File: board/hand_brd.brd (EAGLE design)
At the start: 61.9 x 76.2 mm, 131 parts, among them IC1 FT230XS, Q1 BC847ALT1SMD, Q2 16MHz, Q3 16MHz, U2 ATXMEGA128D4-AU

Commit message: Add missing diode
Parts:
- added U$26: PMEG2010ET, pol:SOT23
- moved R20 2.62 mm to (61.0, 24.1)
- moved R19 1.27 mm to (57.8, 21.6)
- moved Q2 1.27 mm to (54.0, 26.0)
- moved R17 0.90 mm to (60.3, 19.7), turned to 225 degrees
- moved R18 0.63 mm to (55.9, 21.6)
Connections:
- new net N$11: R20.2, U$26.3
- net N$14: now also U$26.1; no longer R20.2
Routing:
- net PDI_CK: track 32.3 -> 29.5 mm
- net N$11: track 0.00 -> 2.23 mm
- net P_XTAL1: track 6.74 -> 8.01 mm
- net P_3V3: track 28.0 -> 26.8 mm
- net N$14: track 13.4 -> 12.6 mm
- net PDI_DATA: track 28.9 -> 28.1 mm
- net N$13: track 10.0 -> 10.6 mm
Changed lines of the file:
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@@
 <element name="C12" library="rcl" package="C0805K" value="10u" x="57.785" y="6.985" smashed="yes" rot="MR180"/>
 <element name="R14" library="rcl" package="M0805" value="10k" x="46.355" y="17.78" smashed="yes" rot="R90"/>
-<element name="Q2" library="special" package="QS" value="16MHz" x="55.245" y="26.035" smashed="yes" rot="R180"/>
+<element name="Q2" library="special" package="QS" value="16MHz" x="53.975" y="26.035" smashed="yes" rot="R180"/>
 <element name="C14" library="rcl" package="C0805K" value="27p" x="52.705003125" y="23.495" smashed="yes" rot="MR180"/>
 <element name="C15" library="rcl" package="C0805K" value="27p" x="57.785003125" y="23.494996875" smashed="yes" rot="MR0"/>
@@
 <attribute name="VALUE" x="40.259" y="26.67" size="1.27" layer="27" ratio="10" rot="R270"/>
 </element>
-<element name="R17" library="rcl" package="M0805" value="10k" x="60.96" y="19.05" smashed="yes" rot="MR270"/>
-<element name="R18" library="rcl" package="M0805" value="100" x="56.515" y="21.59" smashed="yes" rot="R270"/>
-<element name="R19" library="rcl" package="M0805" value="100" x="59.055" y="21.59" smashed="yes" rot="R270"/>
-<element name="R20" library="rcl" package="M0805" value="100" x="61.595" y="21.59" smashed="yes" rot="R270"/>
+<element name="R17" library="rcl" package="M0805" value="10k" x="60.325" y="19.685" smashed="yes" rot="MR225"/>
+<element name="R18" library="rcl" package="M0805" value="100" x="55.88" y="21.59" smashed="yes" rot="R270"/>
+<element name="R19" library="rcl" package="M0805" value="100" x="57.785" y="21.59" smashed="yes" rot="R270"/>
+<element name="R20" library="rcl" package="M0805" value="100" x="60.96" y="24.13" smashed="yes" rot="R270"/>
 <element name="R21" library="rcl" package="M0805" value="10k" x="46.355" y="22.225" smashed="yes" rot="R270"/>
 <element name="R13" library="rcl" package="M0805" value="100" x="45.72" y="12.7" smashed="yes" rot="R90"/>
@@
 <element name="U1" library="MicroUSB" package="USB-MICRO-SMD" value="" x="52.07" y="73.025" rot="MR270"/>
 <element name="U3" library="MicroUSB" package="USB-MICRO-SMD" value="" x="53.975" y="1.905" rot="MR90"/>
+<element name="U$26" library="pol" package="SOT23" value="PMEG2010ET" x="60.96" y="20.32"/>
 </elements>
 <signals>
@@
 <via x="57.785" y="52.705" extent="1-16" drill="0.6"/>
 <via x="43.815" y="36.83" extent="1-16" drill="0.6"/>
-<via x="56.515" y="27.94" extent="1-16" drill="0.6"/>
+<via x="58.42" y="26.035" extent="1-16" drill="0.6"/>
 <contactref element="U1" pad="GND1"/>
 <wire x1="53.37" y1="70.325" x2="53.37" y2="69.82" width="0.4064" layer="16"/>
@@
 <contactref element="Q2" pad="1"/>
 <contactref element="U$13" pad="2"/>
-<wire x1="57.785" y1="26.035" x2="56.78500625" y2="25.035" width="0.4064" layer="16"/>
+<wire x1="56.515" y1="26.035" x2="56.78500625" y2="25.035" width="0.4064" layer="16"/>
 <wire x1="56.78500625" y1="25.035" x2="56.785003125" y2="23.494996875" width="0.4064" layer="16"/>
 <wire x1="55.596115625" y1="19.6895375" x2="56.785003125" y2="20.878428125" width="0.4064" layer="16"/>
@@
 <contactref element="Q2" pad="2"/>
 <contactref element="U$13" pad="1"/>
-<wire x1="52.705" y1="26.035" x2="53.705003125" y2="25.035" width="0.4064" layer="16"/>
-<wire x1="53.705003125" y1="25.035" x2="53.705003125" y2="23.495" width="0.4064" layer="16"/>
 <wire x1="55.030428125" y1="20.255225" x2="53.705003125" y2="21.580653125" width="0.4064" layer="16"/>
 <wire x1="53.705003125" y1="21.580653125" x2="53.705003125" y2="23.495" width="0.4064" layer="16"/>
+<wire x1="53.705003125" y1="23.495" x2="53.705003125" y2="25.034996875" width="0.4064" layer="16"/>
+<wire x1="53.705003125" y1="25.034996875" x2="52.705" y2="26.035" width="0.4064" layer="16"/>
+<wire x1="52.705" y1="26.035" x2="51.435" y2="26.035" width="0.4064" layer="16"/>
 </signal>
 <signal name="N$10">
@@
 <wire x1="46.675" y1="18.415" x2="48.26" y2="18.415" width="0.4064" layer="1"/>
 <wire x1="46.355" y1="21.275" x2="46.355" y2="18.73" width="0.4064" layer="1"/>
-<wire x1="56.727484375" y1="18.55816875" x2="58.169315625" y2="20" width="0.4064" layer="16"/>
-<wire x1="58.169315625" y1="20" x2="60.96" y2="20" width="0.4064" layer="16"/>
+<wire x1="56.727484375" y1="18.55816875" x2="58.526065625" y2="20.35675" width="0.4064" layer="16"/>
+<wire x1="58.526065625" y1="20.35675" x2="59.65325" y2="20.35675" width="0.4064" layer="16"/>
 </signal>
 <signal name="HWB">
@@
 <wire x1="59.410653125" y1="15.875" x2="59.69" y2="15.24" width="0.4064" layer="16"/>
 <via x="59.69" y="15.24" extent="1-16" drill="0.6"/>
-<wire x1="56.515" y1="20.64" x2="56.515" y2="19.05" width="0.4064" layer="1"/>
-<wire x1="56.515" y1="19.05" x2="59.69" y2="15.875" width="0.4064" layer="1"/>
 <wire x1="59.69" y1="15.875" x2="59.69" y2="15.24" width="0.4064" layer="1"/>
+<wire x1="55.88" y1="20.64" x2="55.88" y2="19.685" width="0.4064" layer="1"/>
+<wire x1="55.88" y1="19.685" x2="59.69" y2="15.875" width="0.4064" layer="1"/>
 </signal>
 <signal name="N$13">
@@
 <wire x1="59.8398" y1="13.335" x2="60.325" y2="13.335" width="0.4064" layer="16"/>
 <via x="60.325" y="13.335" extent="1-16" drill="0.6"/>
-<wire x1="59.055" y1="20.64" x2="59.055" y2="18.415" width="0.4064" layer="1"/>
-<wire x1="59.055" y1="18.415" x2="60.96" y2="16.51" width="0.4064" layer="1"/>
-<wire x1="60.96" y1="16.51" x2="60.96" y2="13.97" width="0.4064" layer="1"/>
+<wire x1="60.96" y1="15.875" x2="60.96" y2="13.97" width="0.4064" layer="1"/>
 <wire x1="60.96" y1="13.97" x2="60.325" y2="13.335" width="0.4064" layer="1"/>
+<wire x1="57.785" y1="20.64" x2="57.785" y2="19.05" width="0.4064" layer="1"/>
+<wire x1="57.785" y1="19.05" x2="60.96" y2="15.875" width="0.4064" layer="1"/>
 </signal>
 <signal name="PDI_DATA">
@@
 <contactref element="R19" pad="1"/>
 <contactref element="U2" pad="34"/>
-<wire x1="56.515" y1="22.54" x2="59.055" y2="22.54" width="0.4064" layer="1"/>
+<wire x1="55.88" y1="22.54" x2="57.785" y2="22.54" width="0.4064" layer="1"/>
 <wire x1="47.680353125" y1="41.90720625" x2="47.680353125" y2="42.489646875" width="0.4064" layer="1"/>
 <wire x1="47.680353125" y1="42.489646875" x2="46.99" y2="43.18" width="0.4064" layer="1"/>
@@
 <wire x1="46.99" y1="43.18" x2="46.99" y2="40.64" width="0.4064" layer="16"/>
 <via x="53.975" y="29.21" extent="1-16" drill="0.6"/>
-<wire x1="56.515" y1="22.54" x2="56.2" y2="22.54" width="0.4064" layer="1"/>
+<wire x1="55.88" y1="22.54" x2="56.2" y2="22.54" width="0.4064" layer="1"/>
 <wire x1="46.99" y1="40.64" x2="52.705" y2="34.925" width="0.4064" layer="16"/>
 <wire x1="52.705" y1="34.925" x2="52.705" y2="34.29" width="0.4064" layer="16"/>
 <wire x1="52.705" y1="34.29" x2="53.975" y2="33.02" width="0.4064" layer="16"/>
 <wire x1="53.975" y1="33.02" x2="53.975" y2="29.21" width="0.4064" layer="16"/>
-<wire x1="56.2" y1="22.54" x2="55.245" y2="23.495" width="0.4064" layer="1"/>
-<wire x1="55.245" y1="23.495" x2="55.245" y2="27.94" width="0.4064" layer="1"/>
+<wire x1="55.245" y1="23.175" x2="55.245" y2="27.94" width="0.4064" layer="1"/>
 <wire x1="55.245" y1="27.94" x2="53.975" y2="29.21" width="0.4064" layer="1"/>
+<wire x1="55.245" y1="23.175" x2="55.88" y2="22.54" width="0.4064" layer="1"/>
 </signal>
 <signal name="N$14">
 <contactref element="U$13" pad="11"/>
-<contactref element="R20" pad="2"/>
 <wire x1="57.85885625" y1="13.0532" x2="59.48205625" y2="11.43" width="0.4064" layer="16"/>
 <wire x1="59.48205625" y1="11.43" x2="59.69" y2="11.43" width="0.4064" layer="16"/>
 <via x="59.69" y="11.43" extent="1-16" drill="0.6"/>
-<wire x1="61.595" y1="20.64" x2="62.23" y2="20.005" width="0.4064" layer="1"/>
-<wire x1="62.23" y1="20.005" x2="62.23" y2="13.335" width="0.4064" layer="1"/>
+<wire x1="60.325" y1="11.43" x2="59.69" y2="11.43" width="0.4064" layer="1"/>
+<contactref element="U$26" pad="1"/>
+<wire x1="60.01" y1="19.22" x2="60.01" y2="18.73" width="0.4064" layer="1"/>
+<wire x1="60.01" y1="18.73" x2="62.23" y2="16.51" width="0.4064" layer="1"/>
+<wire x1="62.23" y1="16.51" x2="62.23" y2="13.335" width="0.4064" layer="1"/>
 <wire x1="62.23" y1="13.335" x2="60.325" y2="11.43" width="0.4064" layer="1"/>
-<wire x1="60.325" y1="11.43" x2="59.69" y2="11.43" width="0.4064" layer="1"/>
 </signal>
 <signal name="PDI_CK">
@@
 <via x="49.53" y="42.545" extent="1-16" drill="0.6"/>
 <wire x1="49.53" y1="42.545" x2="49.53" y2="39.37" width="0.4064" layer="16"/>
-<wire x1="61.595" y1="22.54" x2="60.96" y2="23.175" width="0.4064" layer="1"/>
-<wire x1="60.96" y1="23.175" x2="60.96" y2="26.035" width="0.4064" layer="1"/>
+<wire x1="60.96" y1="25.08" x2="60.96" y2="26.035" width="0.4064" layer="1"/>
 <wire x1="60.96" y1="26.035" x2="57.15" y2="29.845" width="0.4064" layer="1"/>
 <wire x1="49.53" y1="39.37" x2="55.245" y2="33.655" width="0.4064" layer="16"/>
@@
 <contactref element="U$13" pad="6"/>
 <contactref element="R17" pad="2"/>
-<wire x1="57.85885625" y1="17.426796875" x2="58.532059375" y2="18.1" width="0.4064" layer="16"/>
-<wire x1="58.532059375" y1="18.1" x2="60.96" y2="18.1" width="0.4064" layer="16"/>
+<wire x1="57.85885625" y1="17.426796875" x2="58.847059375" y2="18.415" width="0.4064" layer="16"/>
+<wire x1="58.847059375" y1="18.415" x2="60.325" y2="18.415" width="0.4064" layer="16"/>
+<wire x1="60.325" y1="18.415" x2="60.923246875" y2="19.013246875" width="0.4064" layer="16"/>
+<wire x1="60.923246875" y1="19.013246875" x2="60.996753125" y2="19.013246875" width="0.4064" layer="16"/>
 </signal>
 <signal name="LED_READY">
@@
 <wire x1="53.975" y1="5.715" x2="53.975" y2="4.605" width="0.4064" layer="16"/>
 </signal>
+<signal name="N$11">
+<contactref element="R20" pad="2"/>
+<contactref element="U$26" pad="3"/>
+<wire x1="60.96" y1="23.18" x2="60.96" y2="21.42" width="0.4064" layer="1"/>
+<wire x1="60.96" y1="20.955" x2="60.96" y2="21.42" width="0.4064" layer="1"/>
+</signal>
 </signals>

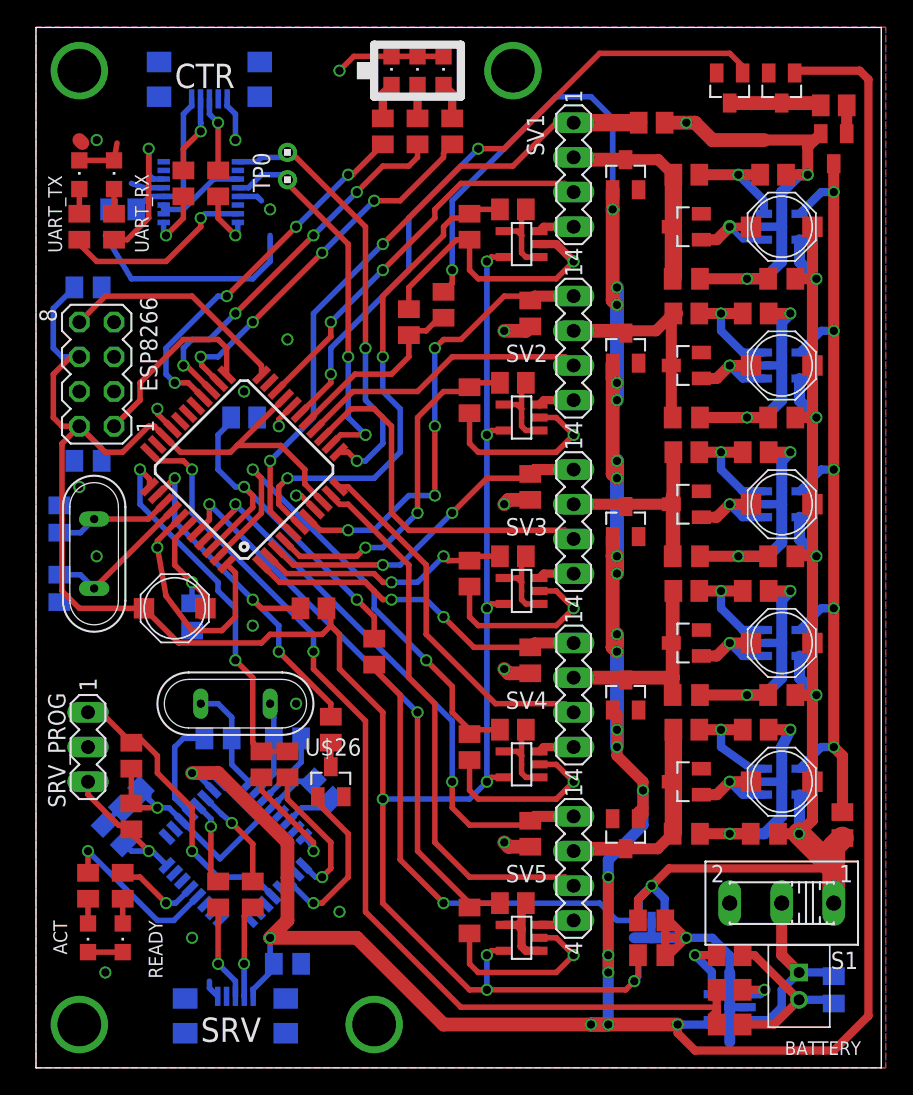
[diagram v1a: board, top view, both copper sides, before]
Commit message: Remove unused connection for disabling the boost converters and shuffle things around a bit to have a better ground plane
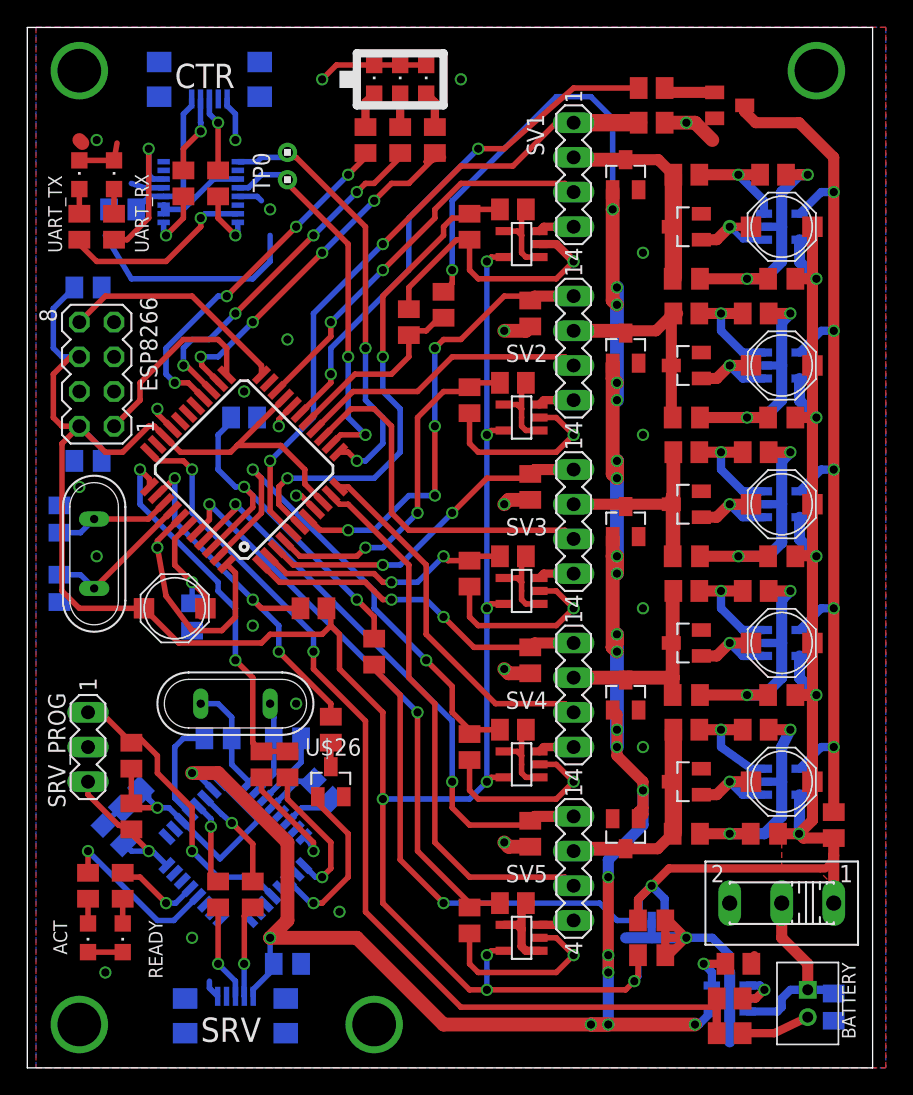
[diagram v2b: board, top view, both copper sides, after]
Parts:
- removed U$11, U$12: PMEG2010ET, pol:SOT23
- moved R12 13.4 mm to (84.5, 71.1)
- moved Q1 8.26 mm to (90.2, 69.8), turned to 270 degrees
- moved HI 1.42 mm to (67.9, 71.8)
- moved BATTERY 1.42 mm to (95.9, 5.08)
- moved LO 1.42 mm to (64.1, 71.8)
- moved MED 1.42 mm to (66.0, 71.8)
- moved R40 1.42 mm to (66.0, 67.3)
- moved R41 1.42 mm to (63.5, 67.3)
- moved R42 1.42 mm to (68.6, 67.3)
- moved C19 1.27 mm to (97.8, 3.81)
- moved R26 0.90 mm to (90.8, 6.99)
- moved U$14 0.64 mm to (90.2, 4.45)
- moved R25 0.64 mm to (90.2, 1.91)
- moved R24 0.63 mm to (90.2, 4.45)
- moved R11 0.63 mm to (97.8, 17.1)
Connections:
- removed net N$6: R12.2, U$11.3, U$12.3
- net BATT_LOW: now also R12.2; no longer U$11.1
- net V_USB_CHG: no longer U$12.1
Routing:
- net V_USB_CHG: track 267.6 -> 177.4 mm
- net GND: track 303.8 -> 286.4 mm, vias 42 -> 47
- net BATT_LOW: track 47.9 -> 38.2 mm
- net S_EN: track 63.6 -> 72.4 mm
- net N$6: track 6.74 -> 0.00 mm
- net N$45: track 28.0 -> 26.0 mm
- net N$5: track 2.07 -> 3.80 mm
- net N$20: track 4.96 -> 3.43 mm
- net N$44: track 27.4 -> 26.1 mm
- net N$46: track 27.5 -> 28.2 mm
- added copper zone on layer 1, net VB
